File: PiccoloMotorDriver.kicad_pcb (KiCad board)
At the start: 2 copper layers, 1 part, among them U1 DRV8316RRGFR

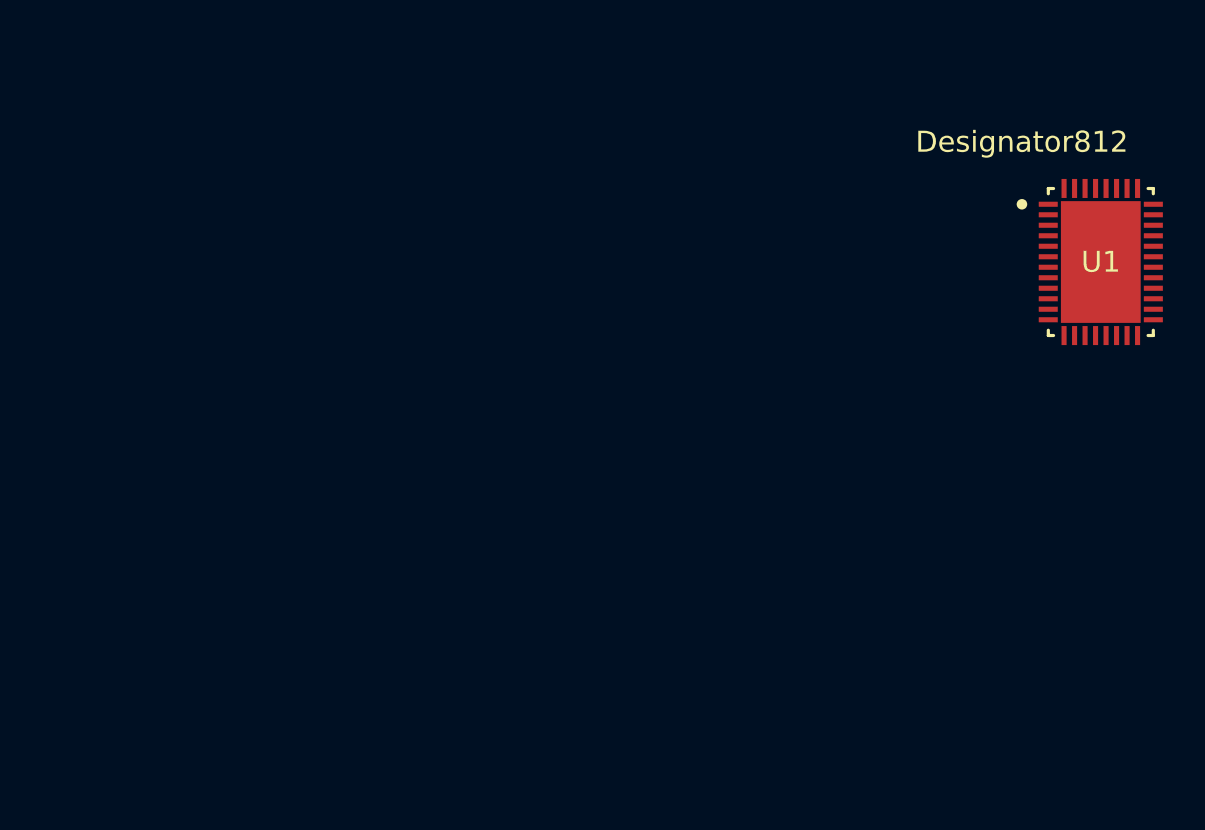
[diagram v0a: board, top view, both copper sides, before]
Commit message: add IO, MCU, power sheets
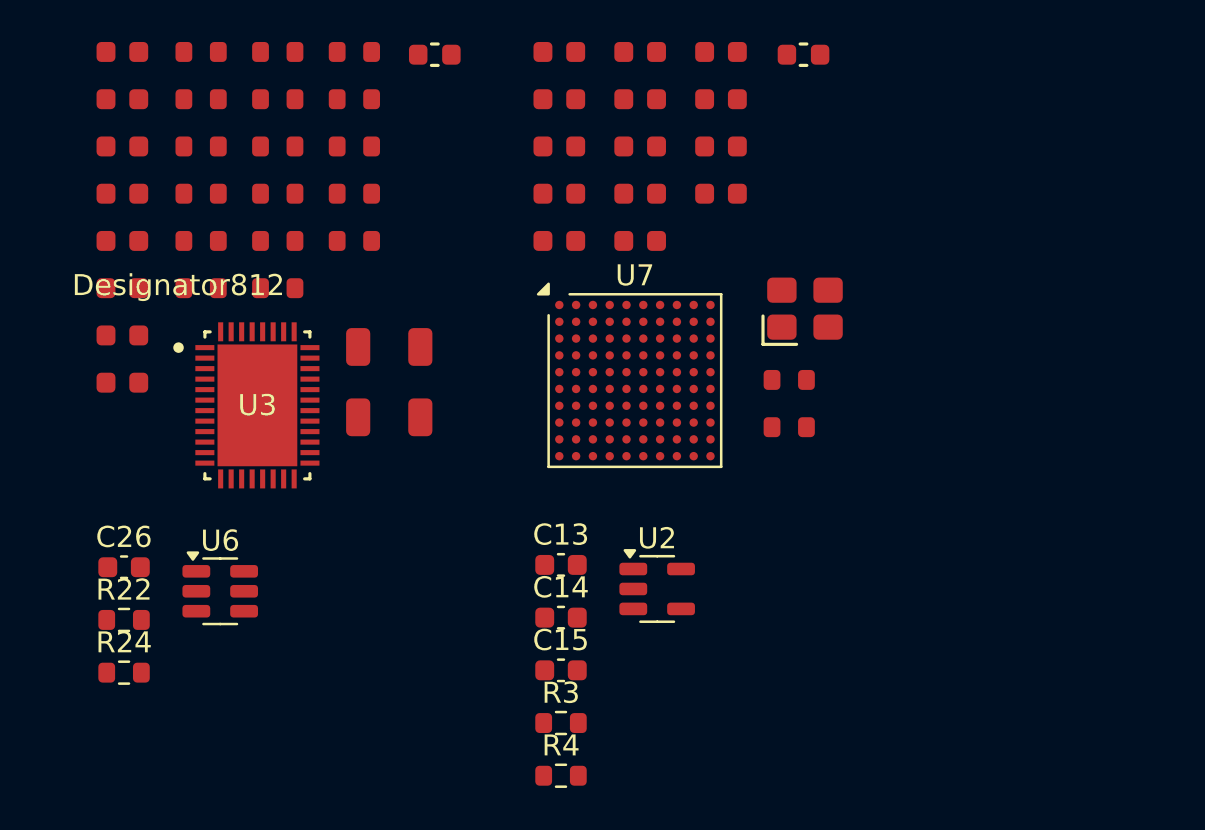
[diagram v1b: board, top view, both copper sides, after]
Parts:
- removed U1: DRV8316RRGFR, DRV8316:RGF0040E-IPC_A
- added C1: 2.2uF, PCM_JLCPCB:C_0603, F.Cu at (125.6, 81.0)
- added C10: 10uF, PCM_JLCPCB:C_1206, F.Cu at (117.5, 98.4)
- added C11: 100nF, PCM_JLCPCB:C_0603, F.Cu at (104.8, 87.8)
- added C12: 100nF, PCM_JLCPCB:C_0603, F.Cu at (104.8, 90.0)
- added C13: 100nF/0603, Capacitor_SMD:C_0603_1608Metric, F.Cu at (125.7, 105.5)
- added C14: 100nF/0603, Capacitor_SMD:C_0603_1608Metric, F.Cu at (125.7, 108.0)
- added C15: 10uF/0603, Capacitor_SMD:C_0603_1608Metric, F.Cu at (125.7, 110.5)
- added C16: 1uF, PCM_JLCPCB:C_0603, F.Cu at (104.8, 92.3)
- added C17: 100nF, PCM_JLCPCB:C_0603, F.Cu at (104.8, 94.5)
- added C18: 47nF, PCM_JLCPCB:C_0603, F.Cu at (104.8, 96.8)
- added C2: 2.2uF, PCM_JLCPCB:C_0603, F.Cu at (125.6, 83.3)
- added C26: 100nF/0603, Capacitor_SMD:C_0603_1608Metric, F.Cu at (104.9, 105.6)
- added C28: 100nF, PCM_JLCPCB:C_0603, F.Cu at (129.4, 81.0)
- added C29: 1uF, PCM_JLCPCB:C_0603, F.Cu at (129.4, 83.3)
- added C3: 100nF, PCM_JLCPCB:C_0603, F.Cu at (125.6, 85.5)
- added C30: 100nF, PCM_JLCPCB:C_0603, F.Cu at (129.4, 85.5)
- added C31: 100nF, PCM_JLCPCB:C_0603, F.Cu at (129.4, 87.8)
- added C32: 100nF, PCM_JLCPCB:C_0603, F.Cu at (129.4, 90.0)
- added C33: 100nF, PCM_JLCPCB:C_0603, F.Cu at (133.3, 81.0)
- added C34: 100nF, PCM_JLCPCB:C_0603, F.Cu at (133.3, 83.3)
- added C35: 100nF, PCM_JLCPCB:C_0603, F.Cu at (133.3, 85.5)
- added C36: 1uF, PCM_JLCPCB:C_0603, F.Cu at (133.3, 87.8)
- added C4: 1nF, PCM_JLCPCB:C_0603, F.Cu at (104.8, 81.0)
- added C5: 1nF, PCM_JLCPCB:C_0603, F.Cu at (104.8, 83.3)
- added C6: 1nF, PCM_JLCPCB:C_0603, F.Cu at (104.8, 85.5)
- added C7: 10uF, PCM_JLCPCB:C_1206, F.Cu at (117.5, 95.1)
- added C8: 10pF, PCM_JLCPCB:C_0603, F.Cu at (125.6, 87.8)
- added C9: 10pF, PCM_JLCPCB:C_0603, F.Cu at (125.6, 90.0)
- added FB1: ~, PCM_JLCPCB:FB_0603, F.Cu at (119.7, 81.2)
- added FB2: ~, PCM_JLCPCB:FB_0603, F.Cu at (137.2, 81.2)
- added R1: 10kΩ, PCM_JLCPCB:R_0603, F.Cu at (108.5, 81.0)
- added R10: 22Ω, PCM_JLCPCB:R_0603, F.Cu at (112.2, 81.0)
- added R11: 22Ω, PCM_JLCPCB:R_0603, F.Cu at (112.2, 83.3)
- added R12: 22Ω, PCM_JLCPCB:R_0603, F.Cu at (112.2, 85.5)
- added R13: 22Ω, PCM_JLCPCB:R_0603, F.Cu at (112.2, 87.8)
- added R14: 22Ω, PCM_JLCPCB:R_0603, F.Cu at (112.2, 90.0)
- added R15: 22Ω, PCM_JLCPCB:R_0603, F.Cu at (112.2, 92.3)
- added R16: 22Ω, PCM_JLCPCB:R_0603, F.Cu at (115.8, 81.0)
- added R17: 22Ω, PCM_JLCPCB:R_0603, F.Cu at (115.8, 83.3)
- added R18: 22Ω, PCM_JLCPCB:R_0603, F.Cu at (115.8, 85.5)
- added R19: 22Ω, PCM_JLCPCB:R_0603, F.Cu at (115.8, 87.8)
- added R2: 22Ω, PCM_JLCPCB:R_0603, F.Cu at (108.5, 83.3)
- added R20: 22Ω, PCM_JLCPCB:R_0603, F.Cu at (115.8, 90.0)
- added R22: 120, Resistor_SMD:R_0603_1608Metric, F.Cu at (104.9, 108.1)
- added R24: 120, Resistor_SMD:R_0603_1608Metric, F.Cu at (104.9, 110.6)
- added R25: 10kΩ, PCM_JLCPCB:R_0603, F.Cu at (136.5, 96.7)
- added R26: 22Ω, PCM_JLCPCB:R_0603, F.Cu at (136.5, 98.9)
- added R3: 1K, Resistor_SMD:R_0603_1608Metric, F.Cu at (125.7, 113.0)
- added R4: 0, Resistor_SMD:R_0603_1608Metric, F.Cu at (125.7, 115.5)
- added R5: 1kΩ, PCM_JLCPCB:R_0603, F.Cu at (108.5, 85.5)
- added R6: 1kΩ, PCM_JLCPCB:R_0603, F.Cu at (108.5, 87.8)
- added R7: 1kΩ, PCM_JLCPCB:R_0603, F.Cu at (108.5, 90.0)
- added R9: 22Ω, PCM_JLCPCB:R_0603, F.Cu at (108.5, 92.3)
- added U2: XC6210B332MR, Package_TO_SOT_SMD:SOT-23-5, F.Cu at (130.3, 106.6)
- added U3: DRV8316RRGFR, DRV8316:RGF0040E-IPC_A, F.Cu at (111.2, 97.9)
- added U6: USBLC6-2SC6, Package_TO_SOT_SMD:SOT-23-6, F.Cu at (109.4, 106.7)
- added U7: STM32H723VGHx, Package_BGA:TFBGA-100_8x8mm_Layout10x10_P0.8mm, F.Cu at (129.2, 96.7)
- added X2: X322516MLB4SI, PCM_JLCPCB:OSC-SMD_4P-L3.2-W2.5-BL, F.Cu at (137.3, 93.3)

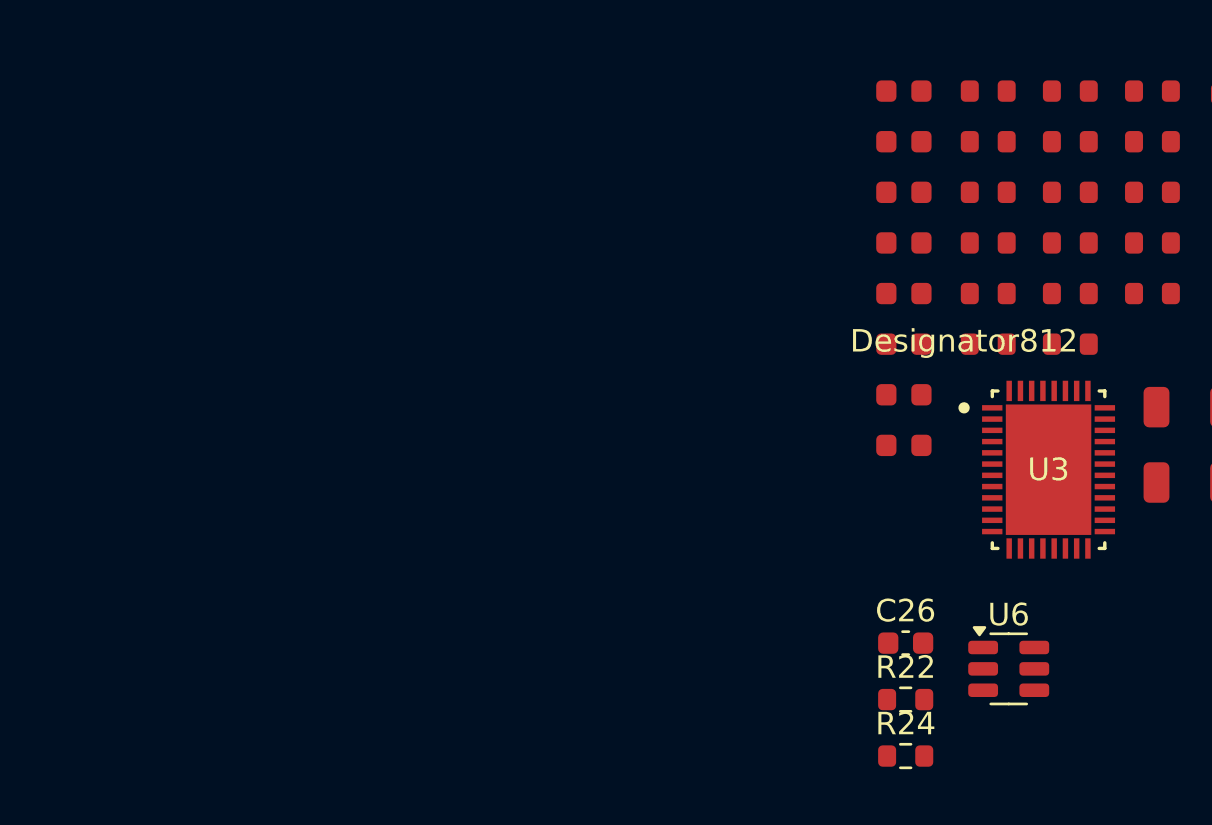
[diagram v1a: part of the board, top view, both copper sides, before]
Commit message: Add mcu connections
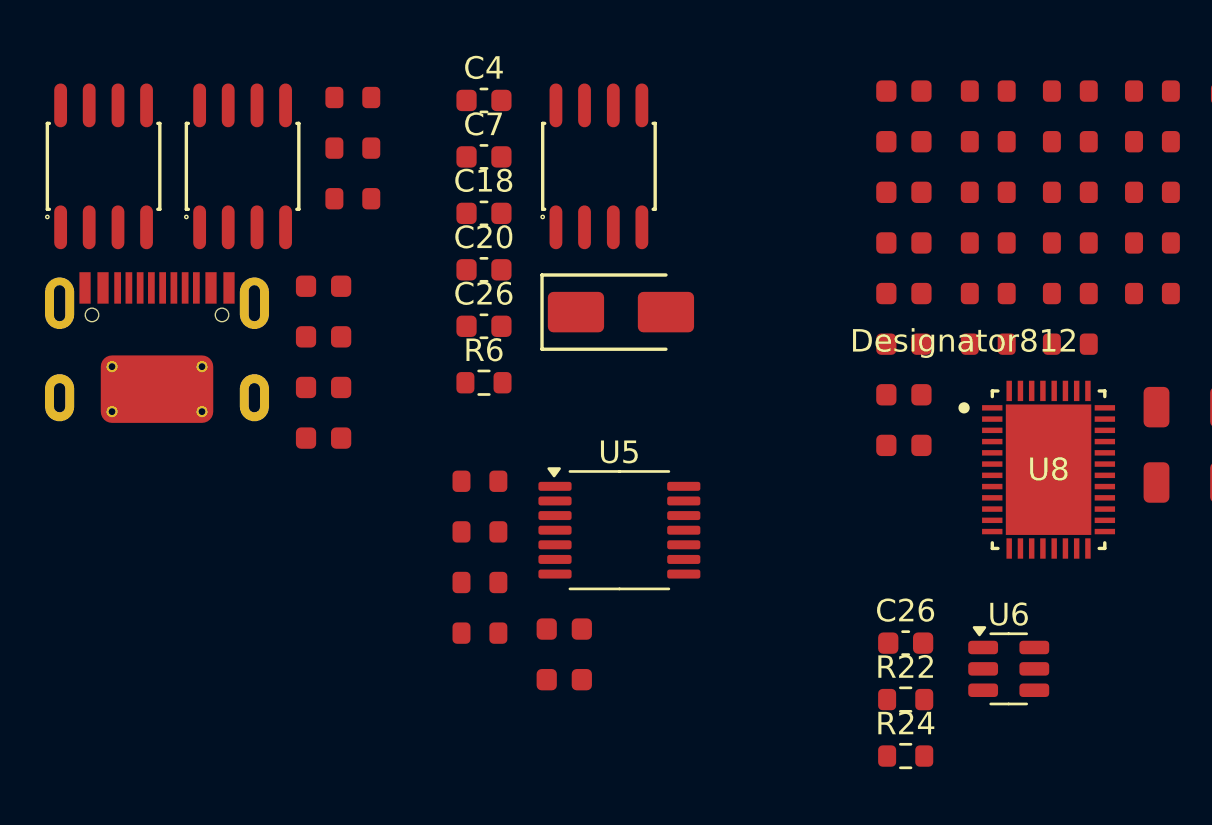
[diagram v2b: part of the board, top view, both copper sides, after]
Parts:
- added C18: 100nF/0603, Capacitor_SMD:C_0603_1608Metric, F.Cu at (86.1, 86.5)
- added C19: 100nF, PCM_JLCPCB:C_0603, F.Cu at (79.0, 89.7)
- added C20: 10uF/0603, Capacitor_SMD:C_0603_1608Metric, F.Cu at (86.1, 89.0)
- added C21: 100nF, PCM_JLCPCB:C_0603, F.Cu at (79.0, 92.0)
- added C22: 100nF, PCM_JLCPCB:C_0603, F.Cu at (79.0, 94.2)
- added C23: 100nF, PCM_JLCPCB:C_0603, F.Cu at (79.0, 96.5)
- added C24: 1uF, PCM_JLCPCB:C_0603, F.Cu at (89.7, 104.9)
- added C25: 100nF, PCM_JLCPCB:C_0603, F.Cu at (89.7, 107.2)
- added C26: 10uF/0603, Capacitor_SMD:C_0603_1608Metric, F.Cu at (86.1, 91.5)
- added C4: 100nF/0603, Capacitor_SMD:C_0603_1608Metric, F.Cu at (86.1, 81.4)
- added C7: 10uF/0603, Capacitor_SMD:C_0603_1608Metric, F.Cu at (86.1, 84.0)
- added D2: US1M, PCM_JLCPCB:D_SMA, F.Cu at (92.2, 90.9)
- added J6: Connector, USB-TYPE-C-16P, PCM_JLCPCB:TYPE-C-SMD_HX-TYPE-C-16PIN, F.Cu at (71.6, 92.3)
- added R21: 10kΩ, PCM_JLCPCB:R_0603, F.Cu at (80.3, 83.6)
- added R22: 120Ω, PCM_JLCPCB:R_0603, F.Cu at (80.3, 85.8)
- added R24: 22Ω, PCM_JLCPCB:R_0603, F.Cu at (85.9, 98.4)
- added R27: 22Ω, PCM_JLCPCB:R_0603, F.Cu at (85.9, 100.6)
- added R28: 22Ω, PCM_JLCPCB:R_0603, F.Cu at (85.9, 102.9)
- added R29: 22Ω, PCM_JLCPCB:R_0603, F.Cu at (85.9, 105.1)
- added R6: 1K, Resistor_SMD:R_0603_1608Metric, F.Cu at (86.1, 94.0)
- added R8: 120Ω, PCM_JLCPCB:R_0603, F.Cu at (80.3, 81.3)
- added U1: SP485EEN, PCM_JLCPCB:SOIC-8_L5.0-W4.0-P1.27-LS6.0-BL, F.Cu at (69.2, 84.4)
- added U3: XL1509, PCM_JLCPCB:SOIC-8_L5.0-W4.0-P1.27-LS6.0-BL, F.Cu at (91.2, 84.4)
- added U4: TJA1050T/CM,118, PCM_JLCPCB:SOIC-8_L5.0-W4.0-P1.27-LS6.0-BL, F.Cu at (75.4, 84.4)
- added U5: AS5047D, Package_SO:TSSOP-14_4.4x5mm_P0.65mm, F.Cu at (92.1, 100.5)
- renumbered C4 to C27, C18 to C37, C7 to C38, R6 to R23, U3 to U8
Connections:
- net Net-(C16-Pad2) renamed Vdrive
- C17 pad 2: GND -> GNDPWR
- C38 pad 2: GND -> GNDPWR
- R4 pad 2: GND -> GNDPWR
- U7 pad A4: unconnected-(U7-PB9-PadA4) -> CAN_TX
- U7 pad A6: unconnected-(U7-PB4(NJTRST)-PadA6) -> ENC_MISO
- U7 pad A7: unconnected-(U7-PB3(JTDO-PadA7) -> ENC_CLK
- U7 pad A8: unconnected-(U7-PA15(JTDI)-PadA8) -> RS485_DE
- U7 pad B10: unconnected-(U7-PA12-PadB10) -> USB+
- U7 pad B4: unconnected-(U7-PB8-PadB4) -> CAN_RX
- U7 pad B8: unconnected-(U7-PC11-PadB8) -> RS485_RO
- U7 pad B9: unconnected-(U7-PC10-PadB9) -> RS485_DI
- U7 pad C10: unconnected-(U7-PA11-PadC10) -> USB-
- U7 pad C5: unconnected-(U7-PB5-PadC5) -> ENC_MOSI
- U7 pad C7: unconnected-(U7-PD3-PadC7) -> DRV_SPI_CLK
- U7 pad C9: unconnected-(U7-PA9-PadC9) -> PWM_B_H
- U7 pad D10: unconnected-(U7-PA10-PadD10) -> PWM_C_H
- U7 pad E2: unconnected-(U7-PC2_C-PadE2) -> DRV_SPI_SDO
- U7 pad F2: unconnected-(U7-PC1-PadF2) -> DRV_SPI_SDI
- U7 pad G10: unconnected-(U7-PB15-PadG10) -> PWM_C_L
- U7 pad G3: unconnected-(U7-PA4-PadG3) -> ENC_CS
- U7 pad G4: unconnected-(U7-PC4-PadG4) -> DRV_AN_REF
- U7 pad G6: unconnected-(U7-PE10-PadG6) -> PWM_B_L
- U7 pad J3: unconnected-(U7-PA6-PadJ3) -> DRV_SO_A
- U7 pad J5: unconnected-(U7-PE8-PadJ5) -> PWM_A_L
- U7 pad K3: unconnected-(U7-PA7-PadK3) -> DRV_SO_B
- U7 pad K4: unconnected-(U7-PB1-PadK4) -> DRV_SO_C
- U7 pad K5: unconnected-(U7-PE9-PadK5) -> PWM_A_H
- U7 pad K8: unconnected-(U7-PB12-PadK8) -> DRV_SPI_~{SCS}
- U8 pad 12: GND -> GNDPWR
- U8 pad 15: GND -> GNDPWR
- U8 pad 18: GND -> GNDPWR
- U8 pad 41: GND -> GNDPWR
